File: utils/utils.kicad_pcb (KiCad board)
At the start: 2 copper layers, 42.2 x 70.5 mm, 24 parts, among them J1 AIN, J2 BIN, J3 GATE, J4 EURORACK_CONN_10, J5 ~OUT, J6 OUT, J7 Conn_01x04, J8 Conn_01x05, U1 TL072, U2 4066, U3 LM317L_TO92, U4 LM337L_TO92

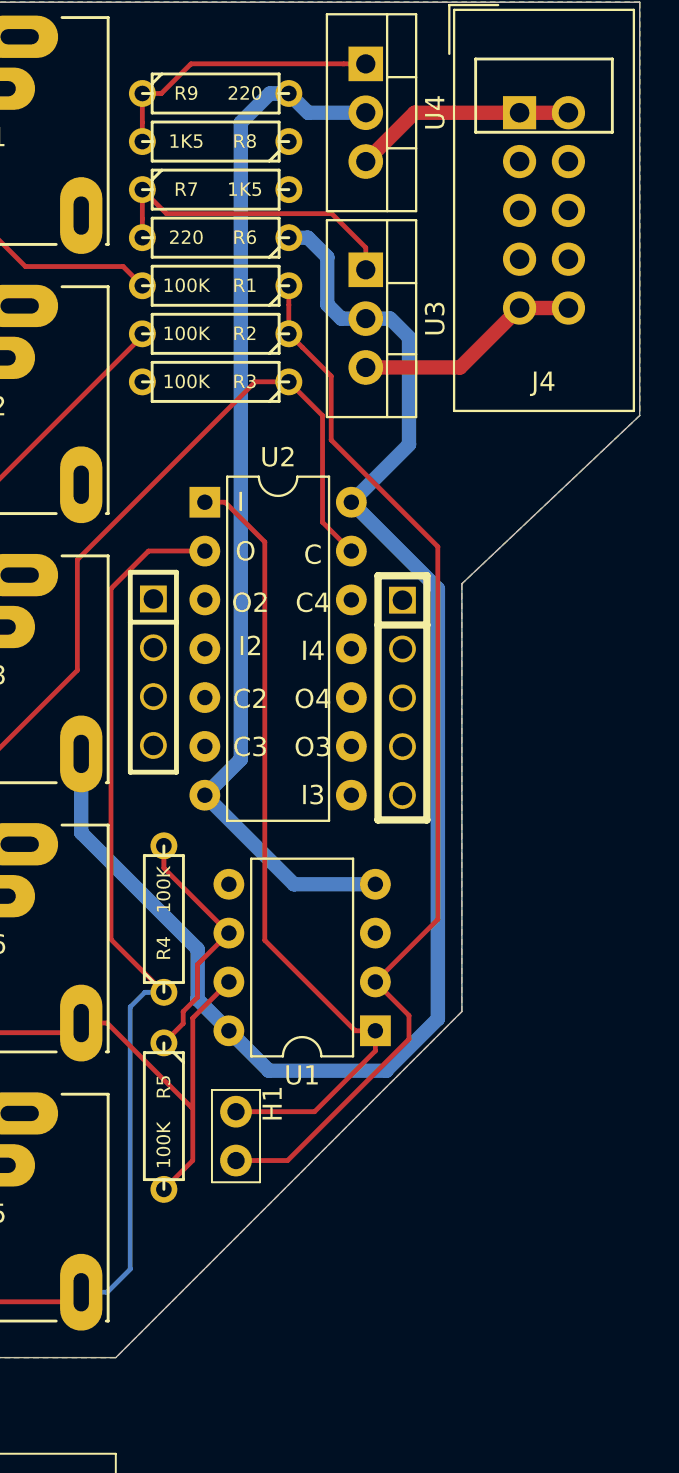
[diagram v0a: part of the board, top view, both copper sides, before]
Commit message: reconnect 4066 headers
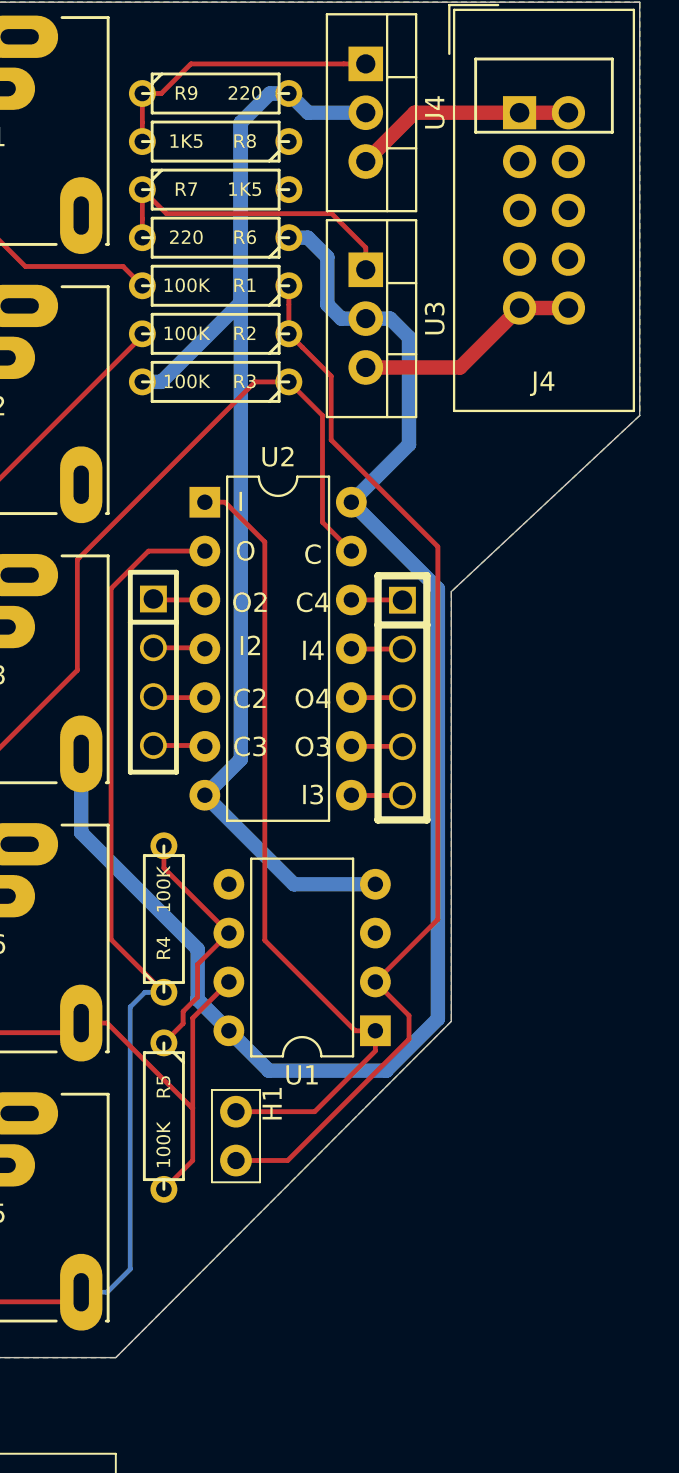
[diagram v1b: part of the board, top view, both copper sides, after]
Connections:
- J7 pad 1: (no net) -> 4066_3
- J7 pad 2: (no net) -> 4066_4
- J7 pad 3: (no net) -> 4066_5
- J7 pad 4: (no net) -> 4066_6
- J8 pad 1: (no net) -> 4066_12
- J8 pad 2: (no net) -> 4066_11
- J8 pad 3: (no net) -> 4066_10
- J8 pad 4: (no net) -> 4066_9
- J8 pad 5: (no net) -> 4066_8
- U2 pad 10: (no net) -> 4066_10
- U2 pad 11: (no net) -> 4066_11
- U2 pad 12: (no net) -> 4066_12
- U2 pad 3: (no net) -> 4066_3
- U2 pad 4: (no net) -> 4066_4
- U2 pad 5: (no net) -> 4066_5
- U2 pad 6: (no net) -> 4066_6
- U2 pad 8: (no net) -> 4066_8
- U2 pad 9: (no net) -> 4066_9
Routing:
- net -10V: track 54.6 -> 70.8 mm
- net 4066_5: track 0.00 -> 2.70 mm
- net 4066_3: track 0.00 -> 2.70 mm
- net 4066_6: track 0.00 -> 2.70 mm
- net 4066_4: track 0.00 -> 2.70 mm
- net 4066_9: track 0.00 -> 2.66 mm
- net 4066_8: track 0.00 -> 2.66 mm
- net 4066_12: track 0.00 -> 2.66 mm
- net 4066_11: track 0.00 -> 2.66 mm
- net 4066_10: track 0.00 -> 2.66 mm
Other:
- outline, holes or cut-outs redrawn

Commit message: rework PCB
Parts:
- removed H1: ?, 4ms/4ms-kicad-lib/lib-footprints/4ms_Connector.pretty:Pins_1x02_2.54mm_TH
- removed R3: 100K, 4ms/4ms-kicad-lib/4ms-footprints.pretty:Resistor_TH_300
- added D1: LED, 4ms/4ms-kicad-lib/4ms-footprints.pretty:LED-3MM-SQUARE-ANODE, F.Cu at (143.8, 62.0)
- added J9: Conn_01x03_Male, 4ms/4ms-kicad-lib/4ms-footprints.pretty:Pin_Header_Straight_1x03, F.Cu at (162.5, 45.7)
- added JP1: Jumper_2_Open, fruchti/fruchtilib/mod/rcl.pretty:SOLDER_JUMPER_0603_B, F.Cu at (143.4, 80.2)
- added JP2: Jumper_2_Open, fruchti/fruchtilib/mod/rcl.pretty:SOLDER_JUMPER_0603_B, F.Cu at (162.4, 87.8)
- added JP3: Jumper_2_Open, fruchti/fruchtilib/mod/rcl.pretty:SOLDER_JUMPER_0603_B, F.Cu at (162.4, 80.2)
- added JP4: Jumper_2_Open, fruchti/fruchtilib/mod/rcl.pretty:SOLDER_JUMPER_0603_B, F.Cu at (143.4, 82.8)
- added JP5: Jumper_2_Open, fruchti/fruchtilib/mod/rcl.pretty:SOLDER_JUMPER_0603_B, F.Cu at (143.4, 85.2)
- added JP6: Jumper_2_Open, fruchti/fruchtilib/mod/rcl.pretty:SOLDER_JUMPER_0603_B, F.Cu at (162.2, 77.8)
- added JP7: Jumper_2_Open, fruchti/fruchtilib/mod/rcl.pretty:SOLDER_JUMPER_0603_B, F.Cu at (143.4, 77.8)
- added JP8: Jumper_2_Open, fruchti/fruchtilib/mod/rcl.pretty:SOLDER_JUMPER_0603_B, F.Cu at (162.4, 85.2)
- added JP9: Jumper_2_Open, fruchti/fruchtilib/mod/rcl.pretty:SOLDER_JUMPER_0603_B, F.Cu at (162.4, 82.8)
- added Q1: 2N3904, 4ms/4ms-kicad-lib/lib-footprints/4ms_Package_TO.pretty:TO-92_OffsetPin2, F.Cu at (143.7, 56.2)
- added R10: 100K, 4ms/4ms-kicad-lib/4ms-footprints.pretty:Resistor_TH_300, F.Cu at (152.9, 67.5)
- added R11: 1K, 4ms/4ms-kicad-lib/4ms-footprints.pretty:Resistor_TH_300, F.Cu at (152.9, 65.0)
- J7: footprint imciner2/KiCad-Libraries/modules/Connectors.pretty:CONN_2.54mm_1x04 -> imciner2/KiCad-Libraries/modules/Connectors.pretty:CONN_2.54mm_1x05
- moved R1 39.6 mm to (145.5, 97.3), turned to 90 degrees
- moved R2 37.0 mm to (142.8, 97.2), turned to 90 degrees
- moved R4 23.5 mm to (163.0, 97.4)
- moved R5 20.1 mm to (160.2, 97.4), turned to 90 degrees
- moved U3 14.7 mm to (161.5, 67.2)
- moved J4 14.5 mm to (144.5, 49.8), turned to 90 degrees
- moved U4 14.5 mm to (161.5, 56.2)
- moved R6 12.1 mm to (152.9, 62.5)
- moved R7 12.1 mm to (152.9, 60.0)
- moved R8 12.1 mm to (152.9, 57.5)
- moved R9 12.1 mm to (152.9, 55.0)
- moved J7 8.06 mm to (146.4, 82.7)
- moved J8 7.34 mm to (159.3, 82.7)
- moved U2 7.34 mm to (149.1, 72.5)
- moved U1 3.91 mm to (149.0, 93.5), turned to 0 degrees
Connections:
- net Net-(RV1-Pad1) renamed STAGE1_OUT
- J3 pad SN: GND -> GATE_CONN
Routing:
- net Net-(R1-Pad1): track 56.1 -> 9.30 mm
- net AIN: track 11.8 -> 48.1 mm
- net GATE_CONN: track 0.00 -> 32.9 mm
- net ~OUT: track 54.2 -> 87.0 mm, vias 0 -> 1
- net STAGE1_OUT: track 42.3 -> 71.1 mm
- net +10V: track 78.8 -> 104.3 mm
- net GATE: track 40.7 -> 65.8 mm
- net Net-(J4-Pad9): track 11.8 -> 32.6 mm
- net Net-(J4-Pad1): track 11.6 -> 31.1 mm
- net BIN: track 14.0 -> 32.7 mm
- net Net-(Q1-Pad1): track 0.00 -> 10.9 mm
- net OUT: track 27.3 -> 33.6 mm
- net Net-(D1-Pad1): track 0.00 -> 5.76 mm
- net -10V: track 70.8 -> 65.5 mm
- net 4066_11: track 2.66 -> 5.10 mm
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- removed copper zone on B.Cu, net GND
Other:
- outline, holes or cut-outs redrawn

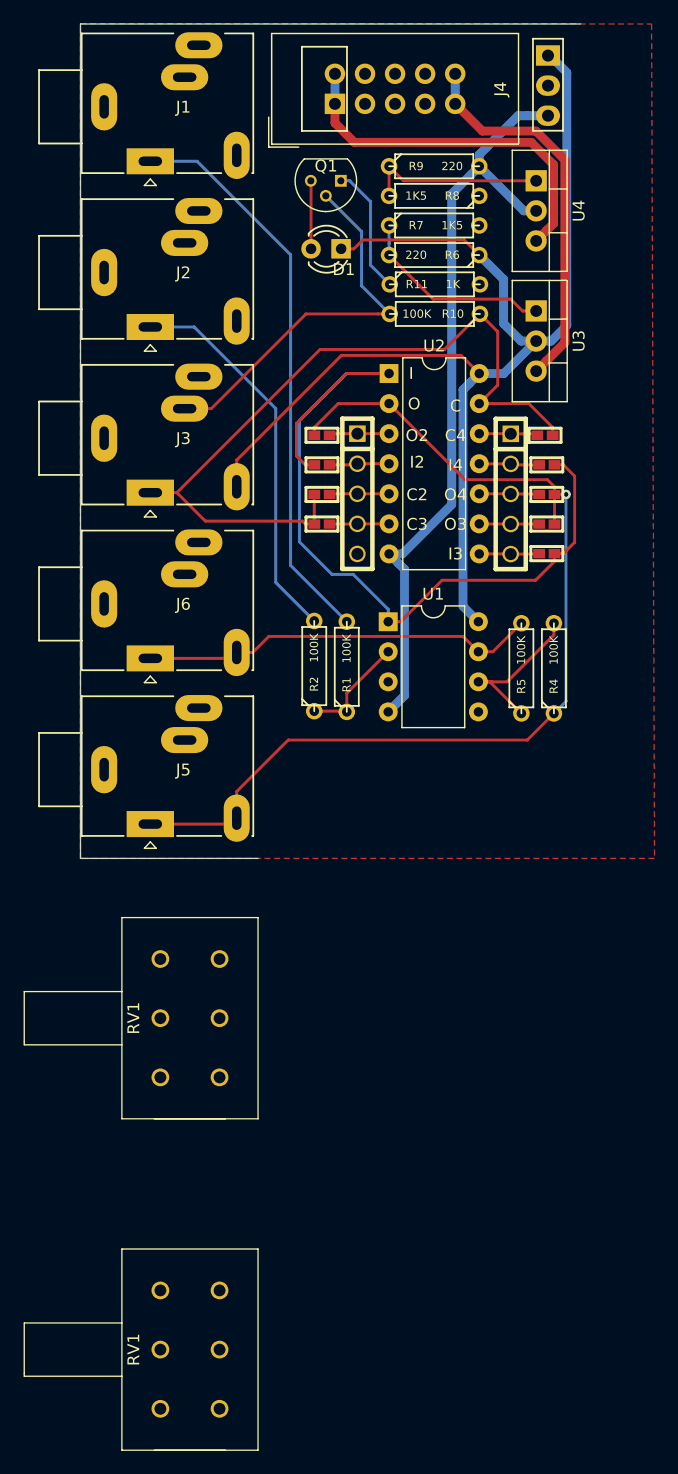
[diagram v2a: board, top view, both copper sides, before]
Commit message: shrunk board  significantly
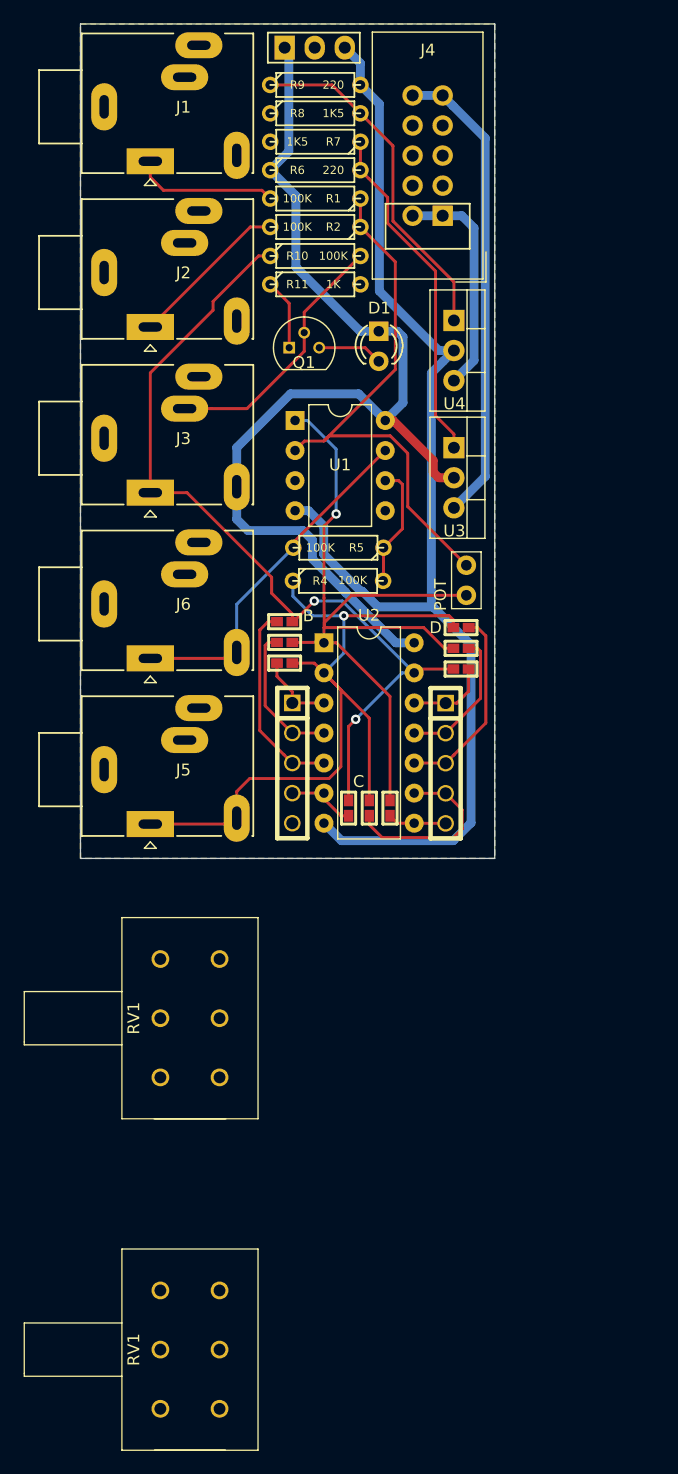
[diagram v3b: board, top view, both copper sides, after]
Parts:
- added POT: ?, 4ms/4ms-kicad-lib/lib-footprints/4ms_Connector.pretty:Pins_1x02_2.54mm_TH, F.Cu at (155.6, 90.0)
- moved R1 39.6 mm to (142.8, 57.8), turned to 180 degrees
- moved R2 37.1 mm to (142.8, 60.1), turned to 180 degrees
- moved JP8 28.3 mm to (147.4, 109.2), turned to 270 degrees
- moved JP2 25.3 mm to (149.2, 109.2), turned to 270 degrees
- moved JP5 24.1 mm to (145.7, 109.2), turned to 270 degrees
- moved J7 23.4 mm to (140.9, 105.4)
- moved J8 23.4 mm to (153.8, 105.5)
- moved U2 23.4 mm to (143.6, 95.3)
- moved J9 22.3 mm to (140.2, 45.0), turned to 90 degrees
- moved JP6 21.0 mm to (155.2, 97.5), turned to 0 degrees
- moved R4 19.7 mm to (144.8, 90.0), turned to 0 degrees
- moved JP7 19.5 mm to (140.2, 97.0), turned to 180 degrees
- moved U1 18.7 mm to (141.1, 76.5)
- moved R5 18.5 mm to (144.8, 87.2), turned to 180 degrees
- moved JP3 17.1 mm to (155.2, 95.8), turned to 0 degrees
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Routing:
- net Net-(R1-Pad1): track 9.30 -> 46.3 mm
- net -10V: track 65.5 -> 102.4 mm
- net AIN: track 48.1 -> 12.2 mm
- net ~OUT: track 87.0 -> 65.8 mm
- net BIN: track 32.7 -> 13.6 mm
- net Net-(R8-Pad2): track 15.4 -> 29.5 mm
- net +10V: track 104.3 -> 91.5 mm
- net Net-(R6-Pad2): track 16.9 -> 29.1 mm
- net Net-(J4-Pad1): track 31.1 -> 19.2 mm
- net 4066_5: track 5.05 -> 16.8 mm
- net 4066_10: track 5.08 -> 16.6 mm
- net GATE_CONN: track 32.9 -> 22.1 mm
- net 4066_9: track 5.06 -> 15.6 mm
- net Net-(J4-Pad9): track 32.6 -> 40.0 mm
- net GATE: track 65.8 -> 73.1 mm, vias 0 -> 2
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- added copper zone on B.Cu, net GND
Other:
- board size 42.2 x 70.5 mm -> 35 x 70.5 mm
- board text added: "B"
- board text added: "D"
- board text removed: "C2"
- board text removed: "C3"
- board text removed: "C4"
- board text removed: "I"
- board text removed: "I2"
- board text removed: "I3"
- board text removed: "I4"
- board text removed: "O"
- board text removed: "O2"
- board text removed: "O3"
- board text removed: "O4"

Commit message: cleanup
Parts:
- moved U1 11.8 mm to (150.5, 83.8), turned to 180 degrees
- moved U3 11.3 mm to (154.5, 67.5)
- moved U4 10.7 mm to (154.5, 78.8)
- moved D1 8.92 mm to (140.0, 73.7)
- moved Q1 5.58 mm to (147.5, 70.6), turned to 270 degrees
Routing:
- net -10V: track 102.4 -> 87.6 mm
- net Net-(R8-Pad2): track 29.5 -> 41.3 mm
- net Net-(R6-Pad2): track 29.1 -> 17.8 mm
- net Net-(J4-Pad9): track 40.0 -> 28.8 mm
- net Net-(J4-Pad1): track 19.2 -> 29.9 mm
- net STAGE1_OUT: track 65.2 -> 54.7 mm, vias 1 -> 0
- net Net-(R1-Pad1): track 46.3 -> 38.0 mm
- net GATE_CONN: track 22.1 -> 27.8 mm
- net +10V: track 91.5 -> 86.4 mm
- net Net-(Q1-Pad1): track 6.01 -> 10.2 mm
- net OUT: track 29.8 -> 25.6 mm
- net Net-(R4-Pad2): track 10.4 -> 13.7 mm
- net Net-(D1-Pad1): track 5.51 -> 8.77 mm
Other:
- board text added: "Rev. A | 2020-05-23"
- board text removed: "BIGASS | Rev. A | 2020-05-23"

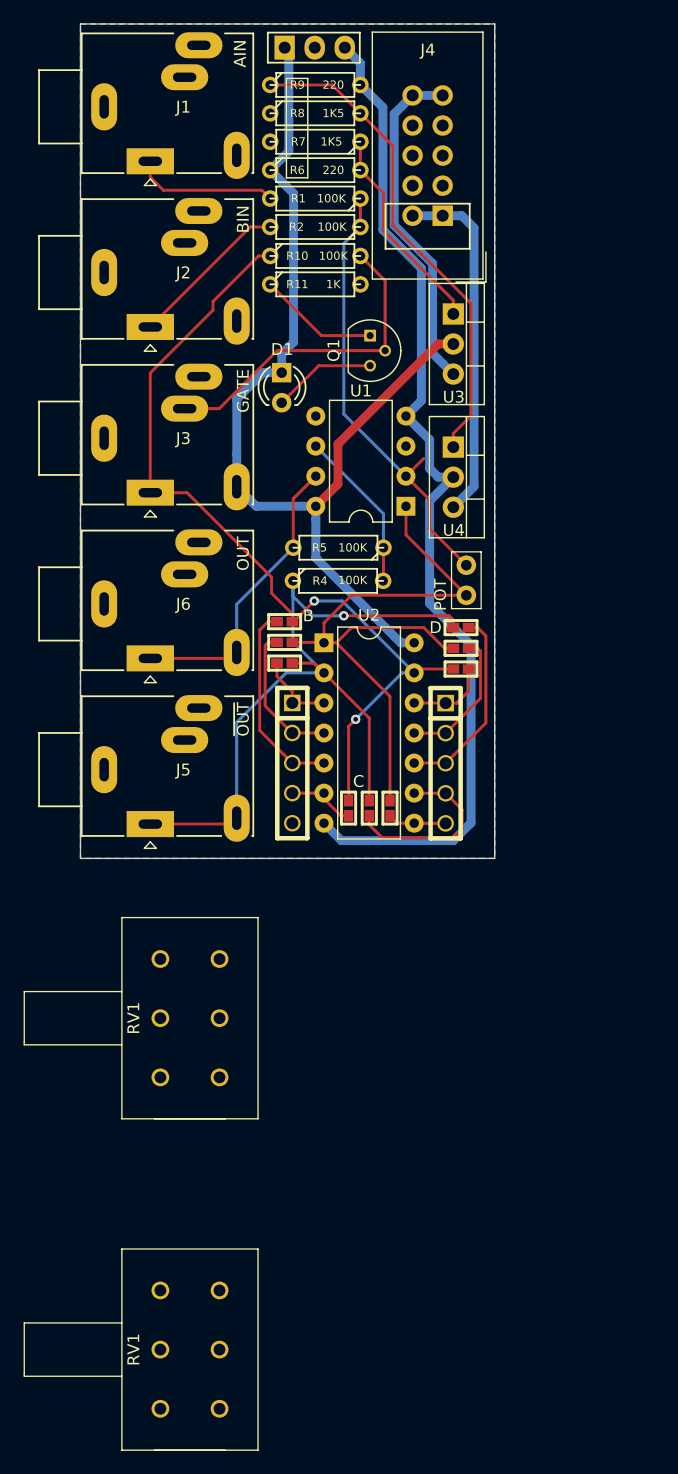
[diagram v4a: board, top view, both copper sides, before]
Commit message: use through-holes for pot
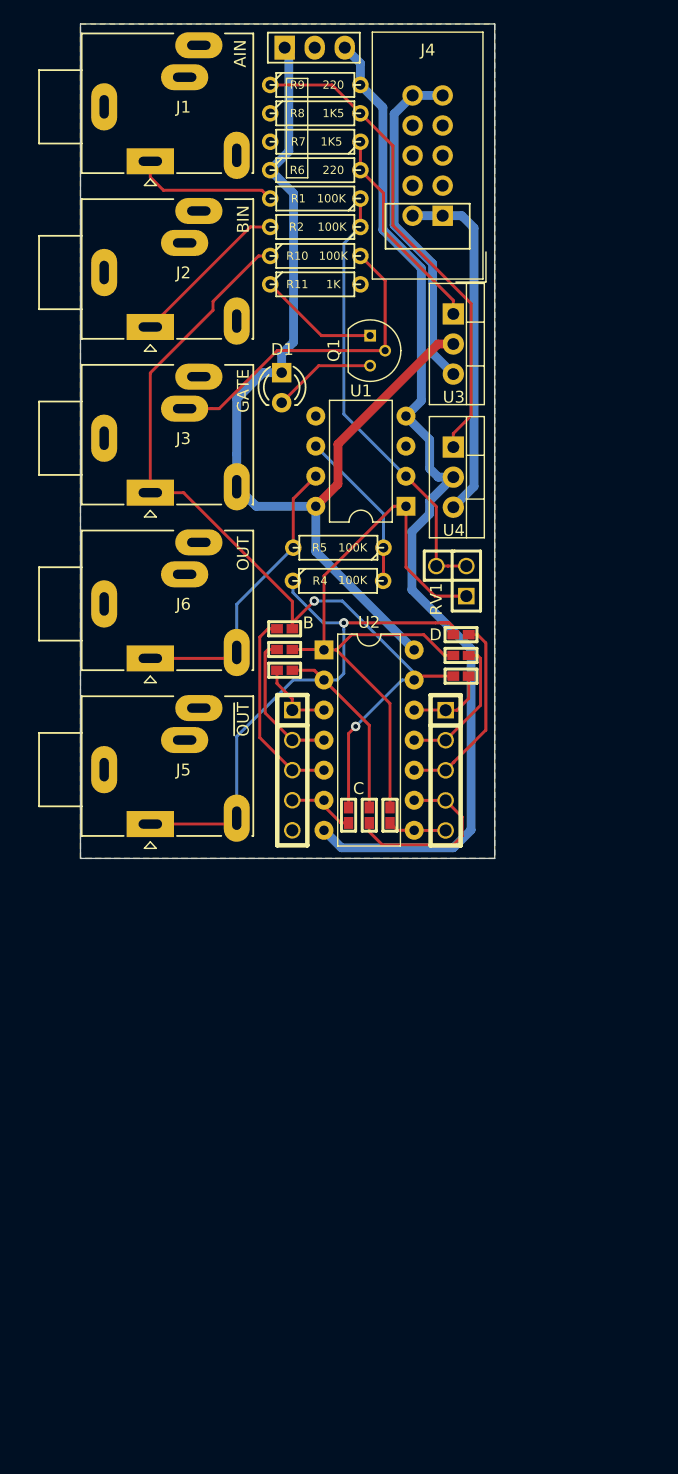
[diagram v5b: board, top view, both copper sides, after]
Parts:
- removed POT: ?, 4ms/4ms-kicad-lib/lib-footprints/4ms_Connector.pretty:Pins_1x02_2.54mm_TH
- removed the RV1 at (132.2, 155.0)
- removed the RV1 at (132.2, 127.0)
- added RV1: 200K, imciner2/KiCad-Libraries/modules/Connectors.pretty:CONN_2.54mm_1x03, F.Cu at (155.6, 88.8)
- moved J7 0.60 mm to (140.9, 106.0)
- moved J8 0.60 mm to (153.8, 106.1)
- moved JP1 0.60 mm to (140.2, 95.8)
- moved JP2 0.60 mm to (149.2, 109.8)
- moved JP3 0.60 mm to (155.2, 96.3)
- moved JP4 0.60 mm to (140.2, 94.1)
- moved JP5 0.60 mm to (145.7, 109.8)
- moved JP6 0.60 mm to (155.2, 98.1)
- moved JP7 0.60 mm to (140.2, 97.6)
- moved JP8 0.60 mm to (147.4, 109.8)
- moved JP9 0.60 mm to (155.2, 94.6)
- moved U2 0.60 mm to (143.6, 95.9)
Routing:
- net ~OUT: track 65.9 -> 62.3 mm
- net STAGE1_OUT: track 54.7 -> 56.9 mm
- net -10V: track 87.6 -> 89.5 mm
- net GATE: track 73.1 -> 74.2 mm
- net Net-(R1-Pad1): track 38.0 -> 37.4 mm
